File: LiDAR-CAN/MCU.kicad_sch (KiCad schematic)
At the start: 0 parts

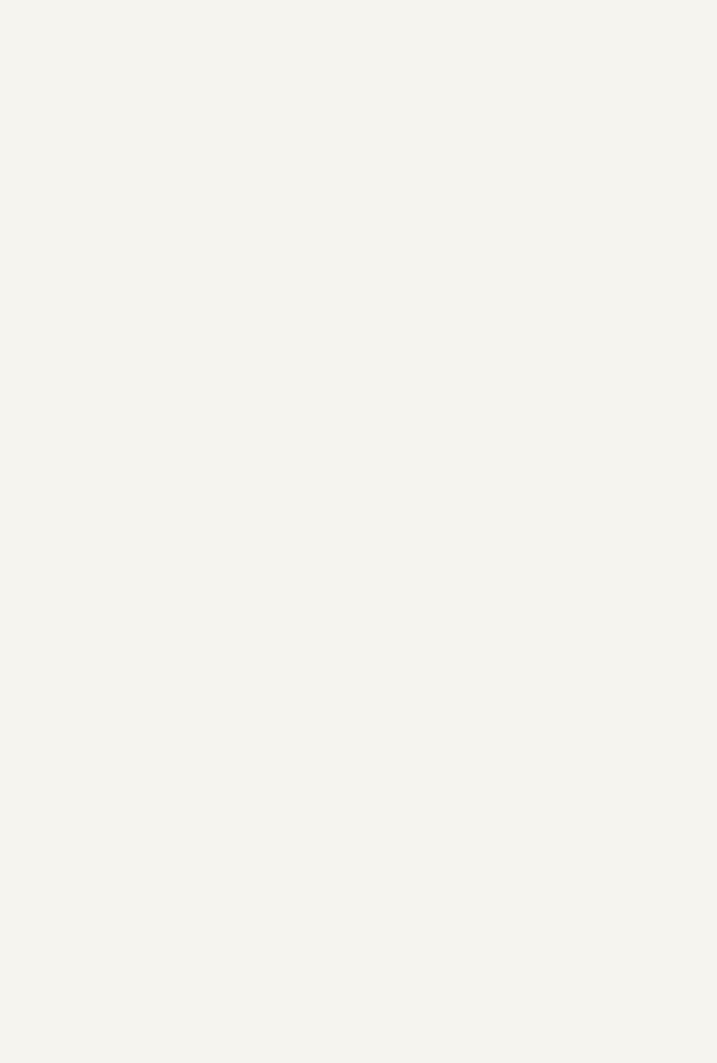
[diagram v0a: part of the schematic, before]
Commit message: Add main components in schematic sheets
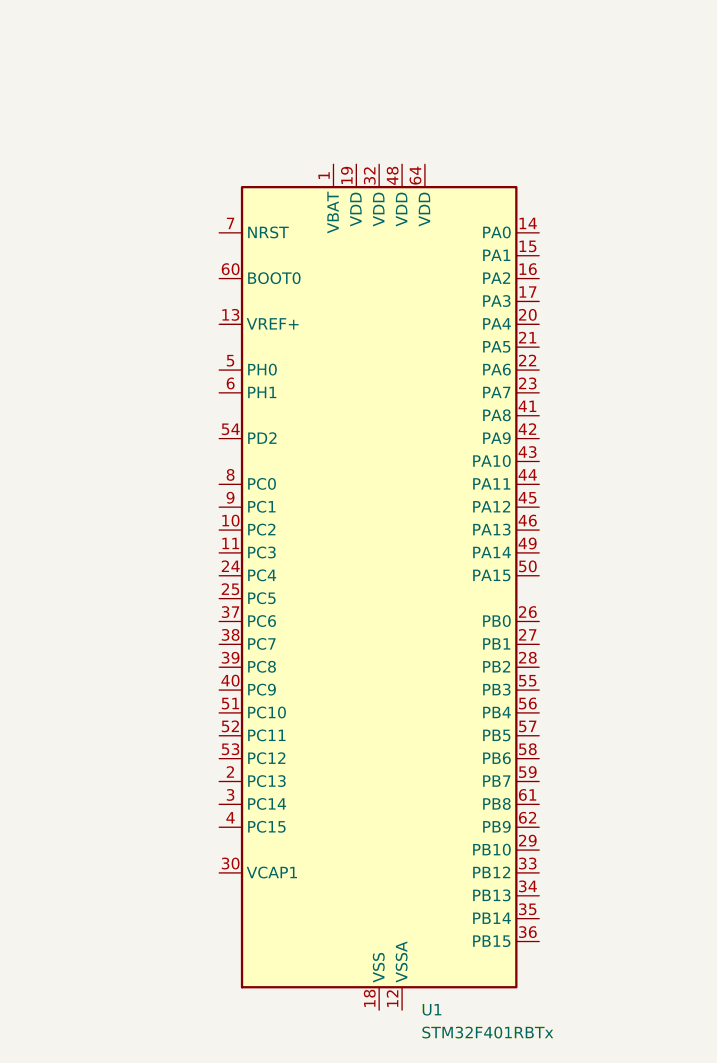
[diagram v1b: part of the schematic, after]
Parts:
- added U1: STM32F401RBTx, Package_QFP:LQFP-64_10x10mm_P0.5mm, symbol MCU_ST_STM32F4:STM32F401RBTx
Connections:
- new net: U1.18 (VSS), U1.31 (VSS), U1.47 (VSS), U1.63 (VSS)
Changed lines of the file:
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@@
+		)
+	)
+	(symbol
+		(lib_id "MCU_ST_STM32F4:STM32F401RBTx")
+		(at 152.4 96.52 0)
+		(unit 1)
+		(exclude_from_sim no)
+		(in_bom yes)
+		(on_board yes)
+		(dnp no)
+		(fields_autoplaced yes)
+		(property "Reference" "U1"
+			(at 157.0833 142.24 0)
+			(effects
+				(font
+					(size 1.27 1.27)
+				)
+				(justify left)
+			)
+		)
+		(property "Value" "STM32F401RBTx"
+			(at 157.0833 144.78 0)
+			(effects
+				(font
+					(size 1.27 1.27)
+				)
+				(justify left)
+			)
+		)
+		(property "Footprint" "Package_QFP:LQFP-64_10x10mm_P0.5mm"
+			(at 137.16 139.7 0)
+			(effects
+				(font
+					(size 1.27 1.27)
+				)
+				(justify right)
+				(hide yes)
+			)
+		)
+		(property "Datasheet" "https://www.st.com/resource/en/datasheet/stm32f401rb.pdf"
+			(at 152.4 96.52 0)
+			(effects
+				(font
+					(size 1.27 1.27)
+				)
+				(hide yes)
+			)
+		)
+		(property "Description" "STMicroelectronics Arm Cortex-M4 MCU, 128KB flash, 64KB RAM, 84 MHz, 1.7-3.6V, 50 GPIO, LQFP64"
+			(at 152.4 96.52 0)
+			(effects
+				(font
+					(size 1.27 1.27)
+				)
+				(hide yes)
+			)
+		)
+		(pin "11"
+		)
+		(pin "25"
+		)
+		(pin "13"
+		)
+		(pin "7"
+		)
+		(pin "60"
+		)
+		(pin "5"
+		)
+		(pin "6"
+		)
+		(pin "54"
+		)
+		(pin "8"
+		)
+		(pin "9"
+		)
+		(pin "10"
+		)
+		(pin "24"
+		)
+		(pin "37"
+		)
+		(pin "14"
+		)
+		(pin "1"
+		)
+		(pin "53"
+		)
+		(pin "21"
+		)
+		(pin "41"
+		)
+		(pin "16"
+		)
+		(pin "30"
+		)
+		(pin "23"
+		)
+		(pin "31"
+		)
+		(pin "40"
+		)
+		(pin "47"
+		)
+		(pin "18"
+		)
+		(pin "52"
+		)
+		(pin "4"
+		)
+		(pin "19"
+		)
+		(pin "38"
+		)
+		(pin "12"
+		)
+		(pin "64"
+		)
+		(pin "51"
+		)
+		(pin "32"
+		)
+		(pin "2"
+		)
+		(pin "63"
+		)
+		(pin "48"
+		)
+		(pin "39"
+		)
+		(pin "3"
+		)
+		(pin "15"
+		)
+		(pin "17"
+		)
+		(pin "20"
+		)
+		(pin "22"
+		)
+		(pin "59"
+		)
+		(pin "43"
+		)
+		(pin "42"
+		)
+		(pin "36"
+		)
+		(pin "44"
+		)
+		(pin "46"
+		)
+		(pin "58"
+		)
+		(pin "62"
+		)
+		(pin "35"
+		)
+		(pin "29"
+		)
+		(pin "45"
+		)
+		(pin "50"
+		)
+		(pin "28"
+		)
+		(pin "55"
+		)
+		(pin "34"
+		)
+		(pin "49"
+		)
+		(pin "26"
+		)
+		(pin "56"
+		)
+		(pin "27"
+		)
+		(pin "57"
+		)
+		(pin "33"
+		)
+		(pin "61"
+		)
+		(instances
+			(project ""
+				(path "/56db6f21-0e4a-4321-bd8a-db37f1842dd9/049d275f-286b-40f8-b875-516fe91bd78e"
+					(reference "U1")
+					(unit 1)
+				)
+			)
 		)
 	)

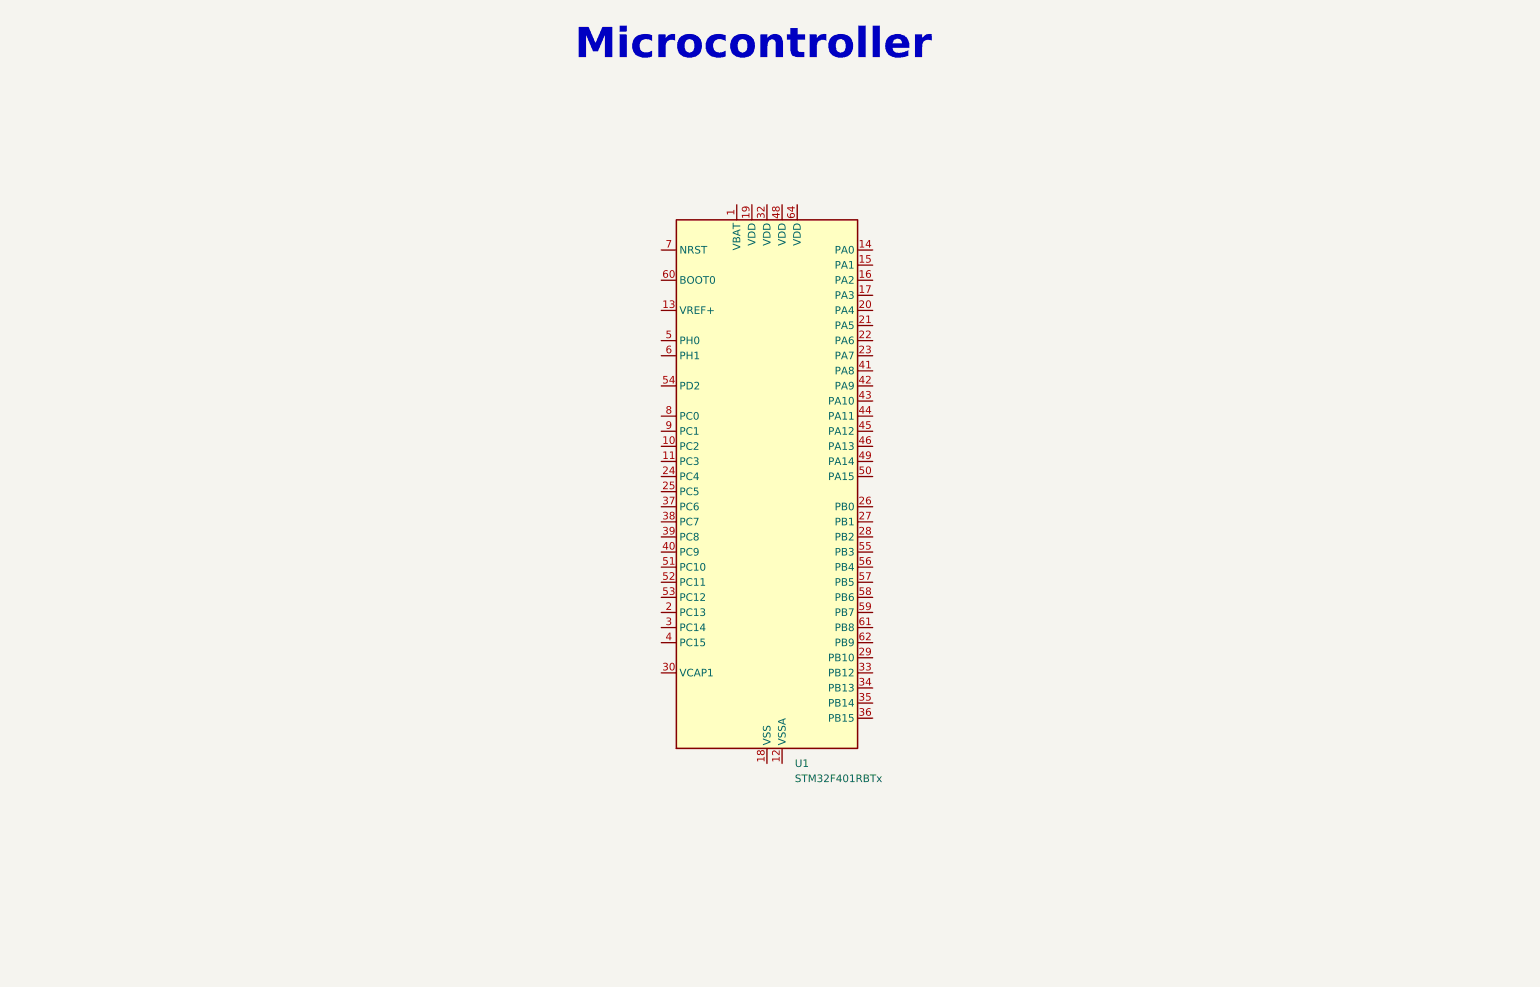
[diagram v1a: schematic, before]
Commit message: Add complete MCU circuit
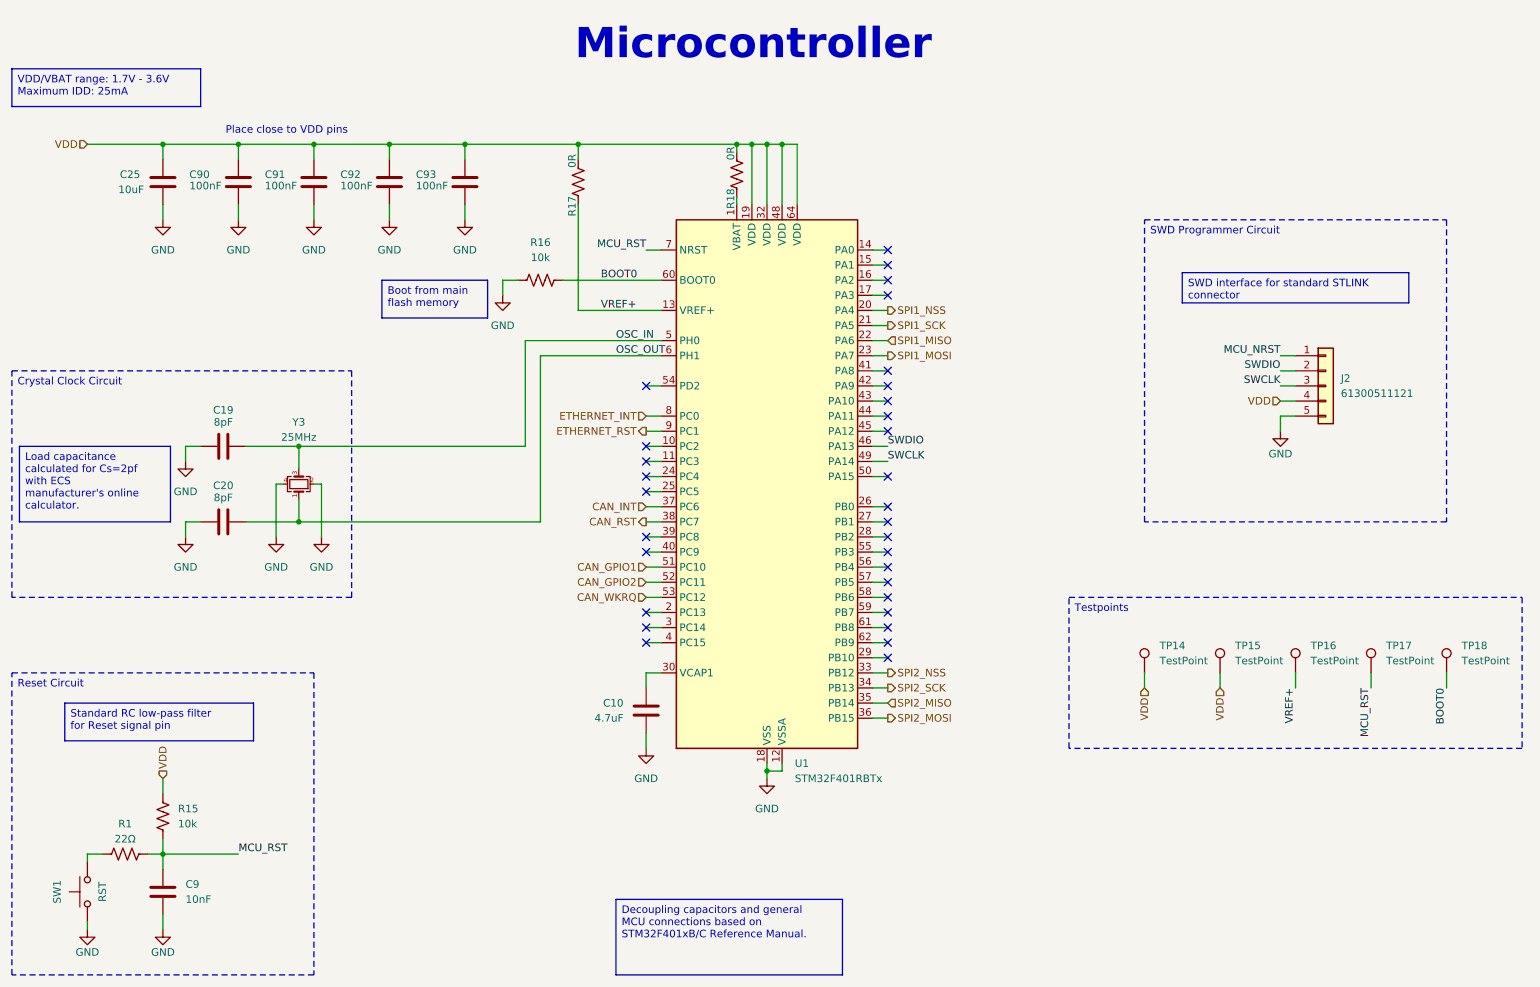
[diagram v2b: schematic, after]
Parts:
- added C10: 4.7uF, Capacitor_SMD:C_0603_1608Metric, symbol Device:C
- added C19, C20: 8pF, Capacitor_SMD:C_0603_1608Metric, symbol Symbols:CAP CER 22PF 50V X7R 0603
- added C25: 10uF, Capacitor_SMD:C_0603_1608Metric, symbol Symbols:CAP CER 10UF 25V X5R 0603
- added C9: 10nF, Capacitor_SMD:C_0603_1608Metric, symbol Device:C
- added C90, C91, C92, C93: 100nF, Capacitor_SMD:C_0603_1608Metric, symbol Symbols:CAP CER 0.1UF 50V X7R 0603
- added J2: 61300511121, Connector_PinHeader_2.54mm:PinHeader_1x05_P2.54mm_Vertical, symbol Connector_Generic:Conn_01x05
- added R1: 22Ω, Resistor_SMD:R_0805_2012Metric, symbol Device:R_US
- added R15, R16: 10k, Resistor_SMD:R_0603_1608Metric, symbol Device:R_US
- added R17, R18: 0R, Resistor_SMD:R_0805_2012Metric, symbol Device:R_US
- added SW1: RST, Button_Switch_SMD:SW_SPST_CK_RS282G05A3, symbol Switch:SW_Push
- added TP14, TP15, TP16, TP17, TP18: TestPoint, TestPoint:TestPoint_Pad_D1.5mm, symbol Connector:TestPoint
- added Y3: 25MHz, Crystal:Crystal_SMD_2016-4Pin_2.0x1.6mm, symbol Device:Crystal_GND24_Small
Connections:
- net at U1.1 (VBAT): now also R18.1
- net GND: now reaches U1.12 (VSSA)
- net GND: now also U1.18 (VSS), U1.31 (VSS), U1.47 (VSS), U1.63 (VSS), C10.2, C19.1, C20.1, C25.2, C9.2, C90.1, C91.1, C92.1, C93.1, J2.5 (Pin_5), R16.2, SW1.1, Y3.2, Y3.4
- net VREF+: now reaches U1.13 (VREF+)
- net VREF+: now also R17.1, TP16.1
- net VDD: now reaches U1.19 (VDD)
- net VDD: now also U1.32 (VDD), U1.48 (VDD), U1.64 (VDD), C25.1, C90.2, C91.2, C92.2, C93.2, J2.4 (Pin_4), R15.1, R17.2, R18.2, TP14.1, TP15.1
- net SPI1_NSS: now reaches U1.20 (PA4)
- net SPI1_SCK: now reaches U1.21 (PA5)
- net SPI1_MISO: now reaches U1.22 (PA6)
- net SPI1_MOSI: now reaches U1.23 (PA7)
- net at U1.30 (VCAP1): now also C10.1
- net SPI2_NSS: now reaches U1.33 (PB12)
- net SPI2_SCK: now reaches U1.34 (PB13)
- net SPI2_MISO: now reaches U1.35 (PB14)
- net SPI2_MOSI: now reaches U1.36 (PB15)
- net CAN_INT: now reaches U1.37 (PC6)
- net CAN_RST: now reaches U1.38 (PC7)
- net SWDIO: now reaches U1.46 (PA13)
- net SWDIO: now also J2.2 (Pin_2)
- net SWCLK: now reaches U1.49 (PA14)
- net SWCLK: now also J2.3 (Pin_3)
- net OSC_IN: now reaches U1.5 (PH0)
- net OSC_IN: now also C19.2, Y3.3
- net CAN_GPIO1: now reaches U1.51 (PC10)
- net CAN_GPIO2: now reaches U1.52 (PC11)
- net CAN_WKRQ: now reaches U1.53 (PC12)
- net OSC_OUT: now reaches U1.6 (PH1)
- net OSC_OUT: now also C20.2, Y3.1
- net BOOT0: now reaches U1.60 (BOOT0)
- net BOOT0: now also R16.1, TP18.1
- net MCU_RST: now reaches U1.7 (NRST)
- net MCU_RST: now also C9.1, R1.2, R15.2, TP17.1
- net ETHERNET_INT: now reaches U1.8 (PC0)
- net ETHERNET_RST: now reaches U1.9 (PC1)
- new net: R1.1, SW1.2
- new net MCU_NRST: J2.1 (Pin_1)
- no-connect marks 0 -> 31
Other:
- note added: "Place close to VDD pins"

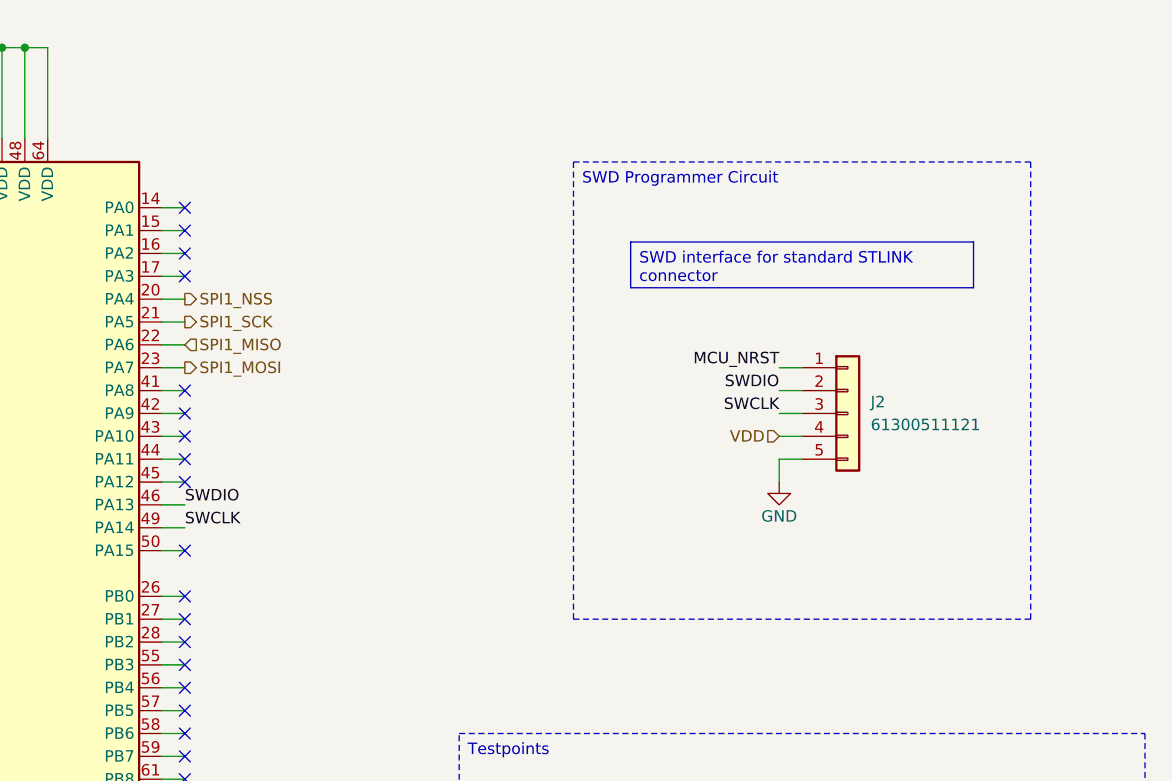
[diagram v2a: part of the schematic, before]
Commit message: Add MCU connections in root sheet
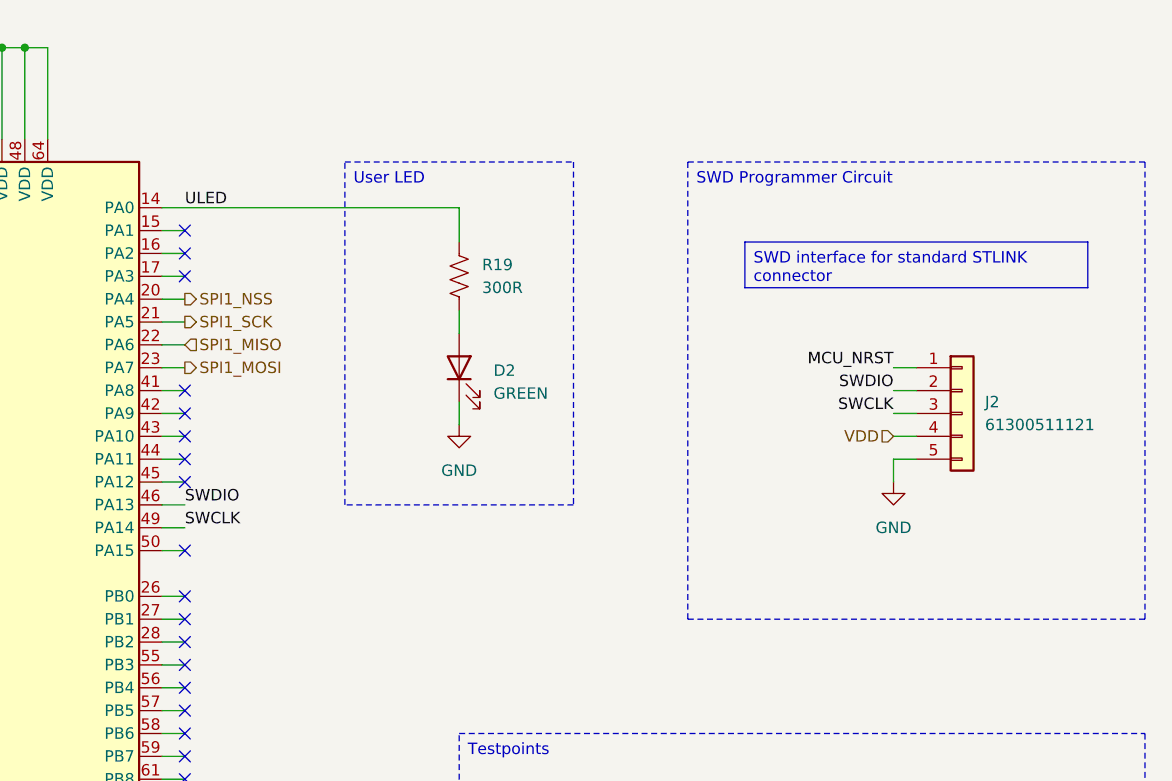
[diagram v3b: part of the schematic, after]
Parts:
- added D2: GREEN, LED_SMD:LED_0603_1608Metric, symbol Device:LED
- added R19: 300R, Resistor_SMD:R_0603_1608Metric, symbol Device:R_US
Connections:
- net GND: now also D2.1 (K)
- net ULED: now reaches U1.14 (PA0)
- net ULED: now also R19.1
- new net: D2.2 (A), R19.2
- no-connect marks 31 -> 30
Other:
- moved on the sheet: J2
